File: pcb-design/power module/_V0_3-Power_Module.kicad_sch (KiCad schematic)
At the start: 11 parts, among them J16 SolarPowerIn and INA219, J17 CN3971, J18 TPS63020-GND-OUT, J19 TPS63020-V-IN, J20 ConnectorHiveScale, J21 MAXS17048, J23 TPS63020-3.3V-OUT, J6 TPS63020-GND-IN

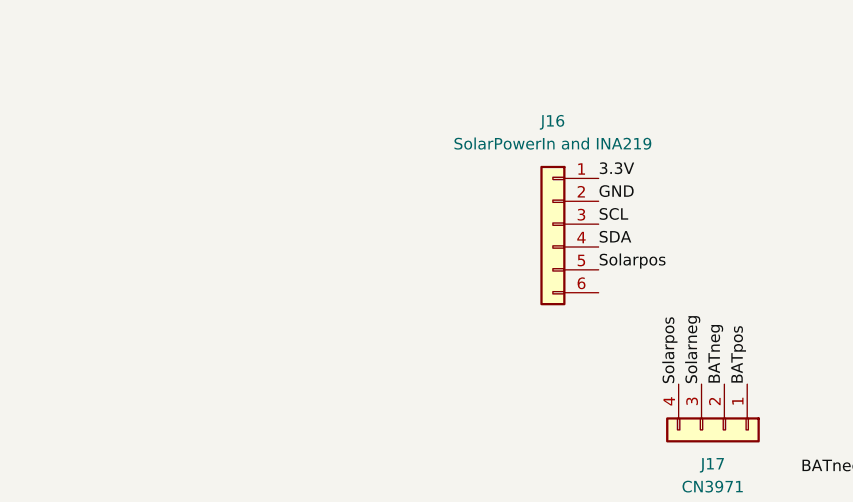
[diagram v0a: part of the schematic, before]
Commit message: added connector for solar panel to power module
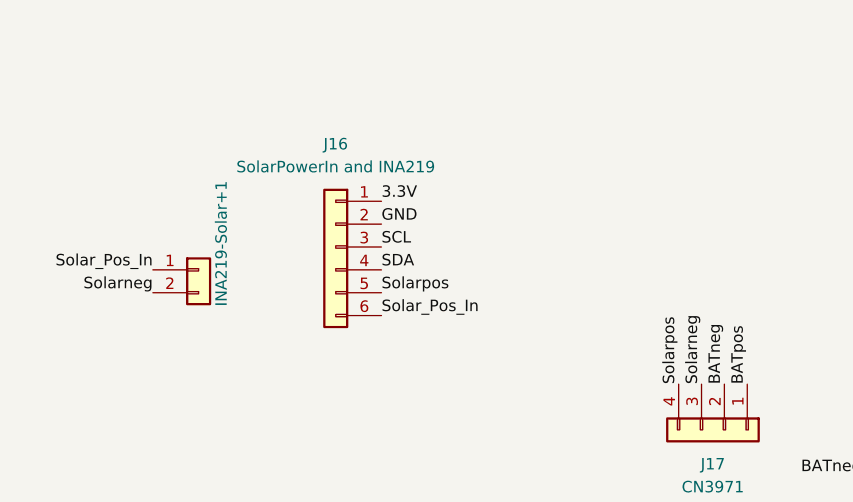
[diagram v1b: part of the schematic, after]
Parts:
- added INA219-Solar+1: Solar_Panel_In, TerminalBlock:TerminalBlock_Xinya_XY308-2.54-2P_1x02_P2.54mm_Horizontal, symbol Connector_Generic:Conn_01x02
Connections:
- net BATneg: now also INA219-Solar+1.2 (Pin_2)
- net Solar_Pos_In: now reaches J16.6 (Pin_6)
- net Solar_Pos_In: now also INA219-Solar+1.1 (Pin_1)
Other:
- moved on the sheet: J16
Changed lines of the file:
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@@
 	)
 	(label "Solarpos"
-		(at 92.71 54.61 0)
+		(at 68.58 57.15 0)
+		(effects
+			(font
+				(size 1.27 1.27)
+			)
+			(justify left bottom)
+		)
+	)
+	(label "Solar_Pos_In"
+		(at 68.58 59.69 0)
 		(effects
 			(font
@@
 		)
 	)
+	(label "Solarneg"
+		(at 43.18 57.15 180)
+		(effects
+			(font
+				(size 1.27 1.27)
+			)
+			(justify right bottom)
+		)
+	)
 	(label "Solarpos"
 		(at 101.6 67.31 90)
@@
 		)
 	)
+	(label "Solar_Pos_In"
+		(at 43.18 54.61 180)
+		(effects
+			(font
+				(size 1.27 1.27)
+			)
+			(justify right bottom)
+		)
+	)
 	(label "3.3V"
-		(at 92.71 44.45 0)
+		(at 68.58 46.99 0)
 		(effects
 			(font
@@
 	)
 	(label "SCL"
-		(at 92.71 49.53 0)
+		(at 68.58 52.07 0)
 		(effects
 			(font
@@
 	)
 	(label "SDA"
-		(at 92.71 52.07 0)
+		(at 68.58 54.61 0)
 		(effects
 			(font
@@
 	)
 	(label "GND"
-		(at 92.71 46.99 0)
+		(at 68.58 49.53 0)
 		(effects
 			(font
@@
 	(symbol
 		(lib_id "Connector_Generic:Conn_01x06")
-		(at 87.63 49.53 0)
+		(at 63.5 52.07 0)
 		(mirror y)
 		(unit 1)
@@
 		(fields_autoplaced yes)
 		(property "Reference" "J16"
-			(at 87.63 38.1 0)
+			(at 63.5 40.64 0)
 			(show_name no)
 			(do_not_autoplace no)
@@
 		)
 		(property "Value" "SolarPowerIn and INA219"
-			(at 87.63 40.64 0)
+			(at 63.5 43.18 0)
 			(show_name no)
 			(do_not_autoplace no)
@@
 		)
 		(property "Footprint" "Connector_PinSocket_2.54mm:PinSocket_1x06_P2.54mm_Vertical"
-			(at 87.63 49.53 0)
+			(at 63.5 52.07 0)
 			(hide yes)
 			(show_name no)
@@
 		)
 		(property "Datasheet" ""
-			(at 87.63 49.53 0)
+			(at 63.5 52.07 0)
 			(hide yes)
 			(show_name no)
@@
 		)
 		(property "Description" "Generic connector, single row, 01x06, script generated (kicad-library-utils/schlib/autogen/connector/)"
-			(at 87.63 49.53 0)
+			(at 63.5 52.07 0)
 			(hide yes)
 			(show_name no)
@@
 					(unit 1)
 				)
+			)
+		)
+	)
+	(symbol
+		(lib_id "Connector_Generic:Conn_01x02")
+		(at 48.26 54.61 0)
+		(unit 1)
+		(body_style 1)
+		(exclude_from_sim no)
+		(in_bom yes)
+		(on_board yes)
+		(in_pos_files yes)
+		(dnp no)
+		(property "Reference" "INA219-Solar+1"
+			(at 50.8 58.674 90)
+			(show_name no)
+			(do_not_autoplace no)
+			(effects
+				(font
+					(size 1.27 1.27)
+				)
+				(justify left)
+			)
+		)
+		(property "Value" "Solar_Panel_In"
+			(at 49.5299 52.07 90)
+			(hide yes)
+			(show_name no)
+			(do_not_autoplace no)
+			(effects
+				(font
+					(size 1.27 1.27)
+				)
+				(justify left)
+			)
+		)
+		(property "Footprint" "TerminalBlock:TerminalBlock_Xinya_XY308-2.54-2P_1x02_P2.54mm_Horizontal"
+			(at 48.26 54.61 0)
+			(hide yes)
+			(show_name no)
+			(do_not_autoplace no)
+			(effects
+				(font
+					(size 1.27 1.27)
+				)
+			)
+		)
+		(property "Datasheet" ""
+			(at 48.26 54.61 0)
+			(hide yes)
+			(show_name no)
+			(do_not_autoplace no)
+			(effects
+				(font
+					(size 1.27 1.27)
+				)
+			)
+		)
+		(property "Description" "Generic connector, single row, 01x02, script generated (kicad-library-utils/schlib/autogen/connector/)"
+			(at 48.26 54.61 0)
+			(hide yes)
+			(show_name no)
+			(do_not_autoplace no)
+			(effects
+				(font
+					(size 1.27 1.27)
+				)
+			)
+		)
+		(pin "1"
+		)
+		(pin "2"
+		)
+		(instances
+			(project "_V0_3-Power_Module"
+				(path "/0fd72f3f-0d89-4c92-9f9e-d7a48828e0f6"
+					(reference "INA219-Solar+1")
+					(unit 1)
+				)

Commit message: updated pcb design
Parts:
- added Bat_Connector: Battery, TerminalBlock:TerminalBlock_Xinya_XY308-2.54-2P_1x02_P2.54mm_Horizontal, symbol Connector_Generic:Conn_01x02
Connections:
- net BATneg: now also Bat_Connector.2 (Pin_2)
- net BATpos: now also Bat_Connector.1 (Pin_1)
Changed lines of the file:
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@@
+		)
+	)
+	(label "BATpos"
+		(at 82.55 97.79 0)
+		(effects
+			(font
+				(size 1.27 1.27)
+			)
+			(justify left bottom)
 		)
 	)
@@
 			)
 			(justify right bottom)
+		)
+	)
+	(label "BATneg"
+		(at 82.55 95.25 0)
+		(effects
+			(font
+				(size 1.27 1.27)
+			)
+			(justify left bottom)
 		)
 	)
@@
 					(unit 1)
 				)
+			)
+		)
+	)
+	(symbol
+		(lib_id "Connector_Generic:Conn_01x02")
+		(at 77.47 97.79 180)
+		(unit 1)
+		(body_style 1)
+		(exclude_from_sim no)
+		(in_bom yes)
+		(on_board yes)
+		(in_pos_files yes)
+		(dnp no)
+		(property "Reference" "Bat_Connector"
+			(at 74.93 93.726 90)
+			(show_name no)
+			(do_not_autoplace no)
+			(effects
+				(font
+					(size 1.27 1.27)
+				)
+				(justify left)
+			)
+		)
+		(property "Value" "Battery"
+			(at 76.2001 100.33 90)
+			(hide yes)
+			(show_name no)
+			(do_not_autoplace no)
+			(effects
+				(font
+					(size 1.27 1.27)
+				)
+				(justify left)
+			)
+		)
+		(property "Footprint" "TerminalBlock:TerminalBlock_Xinya_XY308-2.54-2P_1x02_P2.54mm_Horizontal"
+			(at 77.47 97.79 0)
+			(hide yes)
+			(show_name no)
+			(do_not_autoplace no)
+			(effects
+				(font
+					(size 1.27 1.27)
+				)
+			)
+		)
+		(property "Datasheet" ""
+			(at 77.47 97.79 0)
+			(hide yes)
+			(show_name no)
+			(do_not_autoplace no)
+			(effects
+				(font
+					(size 1.27 1.27)
+				)
+			)
+		)
+		(property "Description" "Generic connector, single row, 01x02, script generated (kicad-library-utils/schlib/autogen/connector/)"
+			(at 77.47 97.79 0)
+			(hide yes)
+			(show_name no)
+			(do_not_autoplace no)
+			(effects
+				(font
+					(size 1.27 1.27)
+				)
+			)
+		)
+		(pin "1"
+		)
+		(pin "2"
+		)
+		(instances
+			(project "_V0_3-Power_Module"
+				(path "/0fd72f3f-0d89-4c92-9f9e-d7a48828e0f6"
+					(reference "Bat_Connector")
+					(unit 1)
+				)
